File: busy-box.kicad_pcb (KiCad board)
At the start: 2 copper layers, 86.2 x 55.8 mm, 18 parts, among them SW1 SW_SPST, SW2 SW_SPST, SW3 SW_SPST, U1 STM32G030F6Px, U2 LM1117MP-3.3

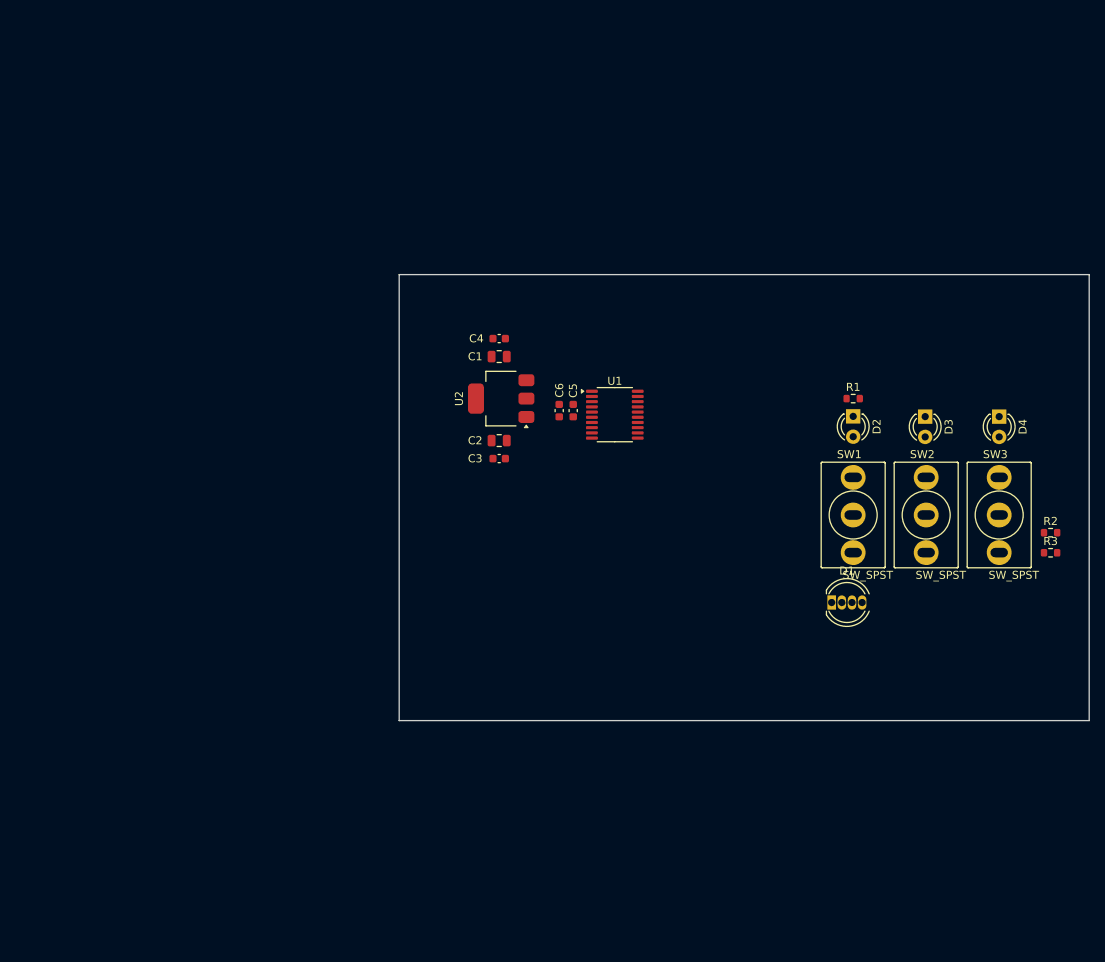
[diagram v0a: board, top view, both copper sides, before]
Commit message: Added sliders
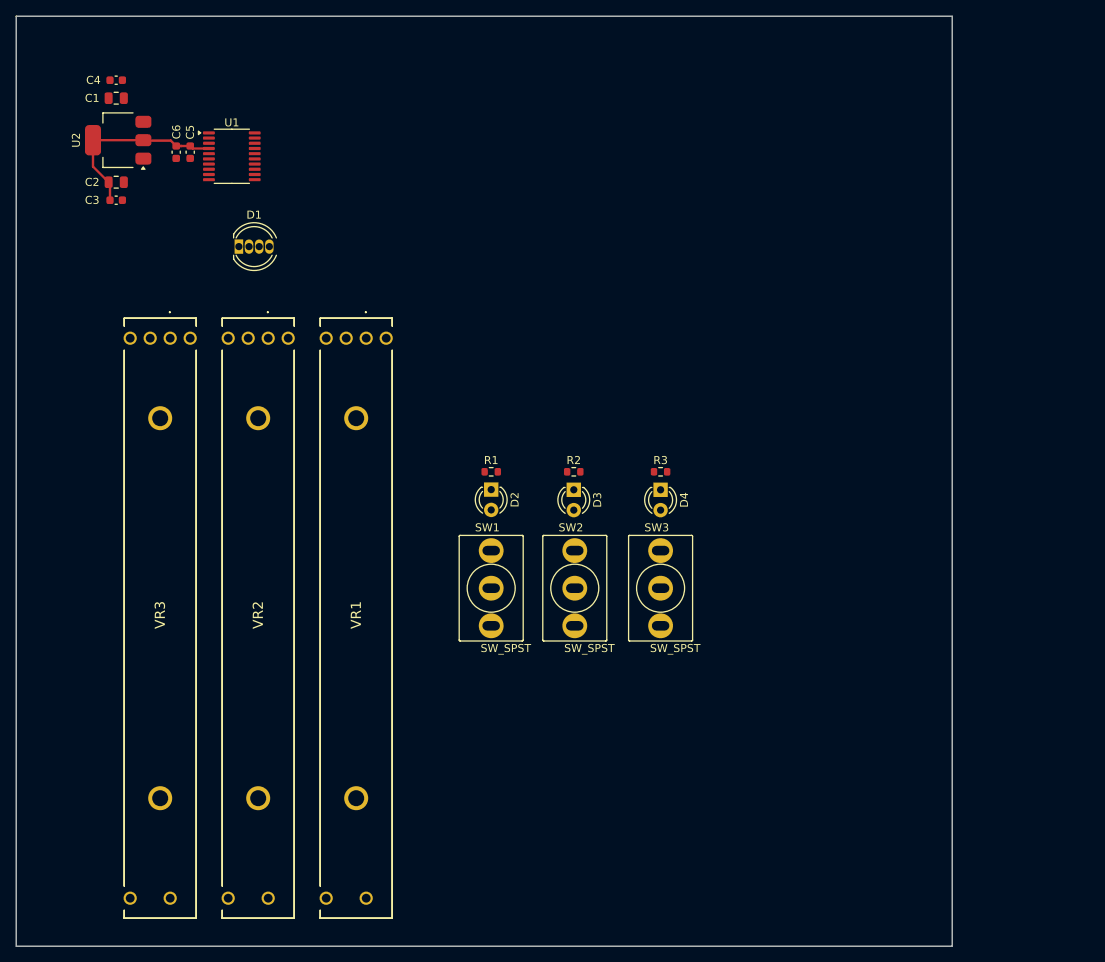
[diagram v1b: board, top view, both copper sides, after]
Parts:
- added VR1: Alps-Slide-Potentiometer-60mm-RS6011SP6003, rhinocerose-pots:Alps-Slide-Pot-60mm-RS6011SP6003, F.Cu at (94.1, 84.0)
- added VR2: Alps-Slide-Potentiometer-60mm-RS6011SP6003, rhinocerose-pots:Alps-Slide-Pot-60mm-RS6011SP6003, F.Cu at (81.9, 84.0)
- added VR3: Alps-Slide-Potentiometer-60mm-RS6011SP6003, rhinocerose-pots:Alps-Slide-Pot-60mm-RS6011SP6003, F.Cu at (69.6, 84.0)
- moved D1 86.4 mm to (78.2, 72.5)
- moved R2 60.1 mm to (120.1, 100.7)
- moved U1 57.8 mm to (77.3, 61.2)
- moved C1 57.8 mm to (62.9, 54.0)
- moved C2 57.8 mm to (62.9, 64.5)
- moved C3 57.8 mm to (62.9, 66.7)
- moved C4 57.8 mm to (62.9, 51.7)
- moved U2 57.8 mm to (63.1, 59.2)
- moved C5 57.8 mm to (72.1, 60.7)
- moved C6 57.8 mm to (70.4, 60.7)
- moved R3 49.8 mm to (130.9, 100.7)
- moved D2 46.2 mm to (109.8, 102.9)
- moved R1 46.2 mm to (109.8, 100.7)
- moved SW1 46.2 mm to (109.8, 115.2)
- moved D3 44.9 mm to (120.1, 102.9)
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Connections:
- D1 pad 1: unconnected-(D1-K-Pad1) -> GND
- SW1 pad 2: +VDC -> +3.3V
- SW2 pad 2: +VDC -> +3.3V
- SW3 pad 2: +VDC -> +3.3V
- U1 pad 7: unconnected-(U1-PA0-Pad7) -> ADC_IN_1
- U1 pad 8: unconnected-(U1-PA1-Pad8) -> ADC_IN_2
- U1 pad 9: unconnected-(U1-PA2-Pad9) -> ADC_IN_3
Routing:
- net +3.3V: track 0.00 -> 23.9 mm
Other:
- board size 86.2 x 55.8 mm -> 117 x 116.2 mm
